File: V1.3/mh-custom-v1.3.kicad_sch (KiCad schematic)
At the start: 0 parts

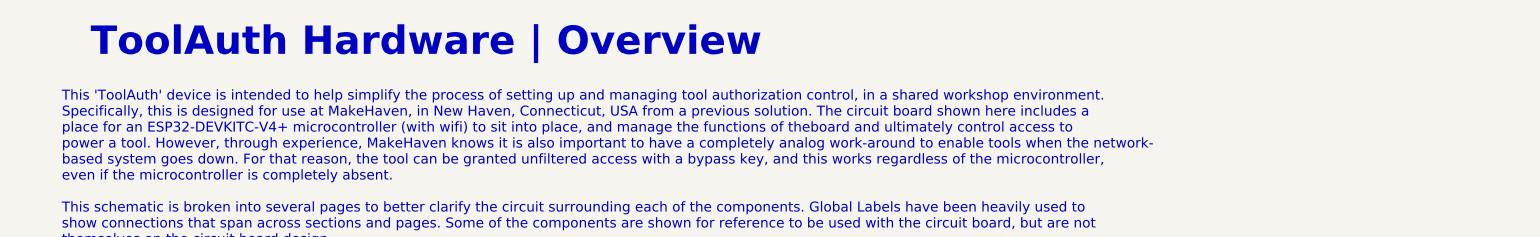
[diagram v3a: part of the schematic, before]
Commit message: clarify door-activator role || Active & Passive door operation
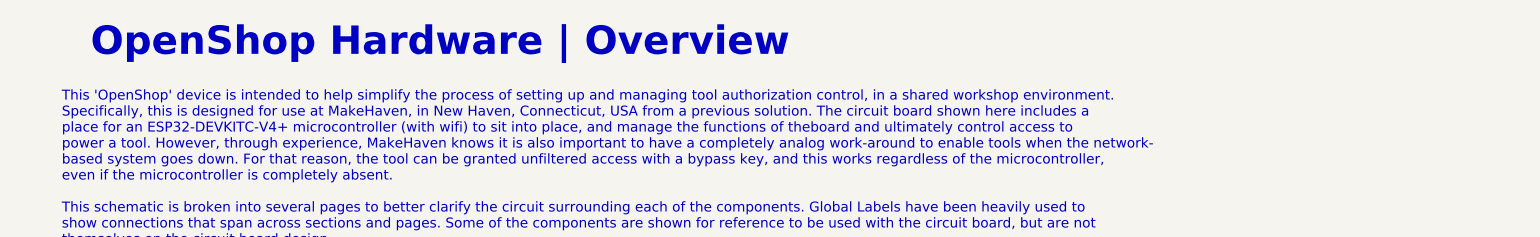
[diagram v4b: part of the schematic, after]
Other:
- note added: "OpenShop Hardware | Overview"
- note added: "This 'OpenShop' device is intended to help simplify the process of setting up and managing tool authorization control, in a shared workshop environment. Specifically, this is designed for use at MakeHaven, in New Haven, Connecticut, USA from a previous solution. The circuit board shown here includes a place for an ESP32-DEVKITC-V4+ microcontroller (with wifi) to sit into place, and manage the fun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"
- note removed: "This 'ToolAuth' device is intended to help simplify the process of setting up and managing tool authorization control, in a shared workshop environment. Specifically, this is designed for use at MakeHaven, in New Haven, Connecticut, USA from a previous solution. The circuit board shown here includes a place for an ESP32-DEVKITC-V4+ microcontroller (with wifi) to sit into place, and manage the fun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"
- note removed: "ToolAuth Hardware | Overview"
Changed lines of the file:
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@@
     (stroke (width 0) (type default) (color 0 0 0 0))
   )
-  (text "ToolAuth Hardware | Overview" (at 40.64 39.37 0)
+  (text "OpenShop Hardware | Overview" (at 40.64 39.37 0)
     (effects (font (size 5 5) (thickness 0.5) bold) (justify left bottom))
   )
@@
     (effects (font (size 1.75 1.75)) (justify left bottom))
   )
-  (text "This 'ToolAuth' device is intended to help simplify the process of setting up and managing tool authorization control, in a shared workshop environment. \nSpecifically, this is designed for use at MakeHaven, in New Haven, Connecticut, USA from a previous solution. The circuit board shown here includes a \nplace for an ESP32-DEVKITC-V4+ microcontroller (with wifi) to sit into place, and manage the functions of theboard and ultimately control access to \npower a tool. However, through experience, MakeHaven knows it is also important to have a completely analog work-around to enable tools when the network-\nbased system goes down. For that reason, the tool can be granted unfiltered access with a bypass key, and this works regardless of the microcontroller, \neven if the microcontroller is completely absent. \n\nThis schematic is broken into several pages to better clarify the circuit surrounding each of the components. Global Labels have been heavily used to \nshow connections that span across sections and pages. Some of the components are shown for reference to be used with the circuit board, but are not \nthemselves on the circuit board design. \n"
+  (text "This 'OpenShop' device is intended to help simplify the process of setting up and managing tool authorization control, in a shared workshop environment. \nSpecifically, this is designed for use at MakeHaven, in New Haven, Connecticut, USA from a previous solution. The circuit board shown here includes a \nplace for an ESP32-DEVKITC-V4+ microcontroller (with wifi) to sit into place, and manage the functions of theboard and ultimately control access to \npower a tool. However, through experience, MakeHaven knows it is also important to have a completely analog work-around to enable tools when the network-\nbased system goes down. For that reason, the tool can be granted unfiltered access with a bypass key, and this works regardless of the microcontroller, \neven if the microcontroller is completely absent. \n\nThis schematic is broken into several pages to better clarify the circuit surrounding each of the components. Global Labels have been heavily used to \nshow connections that span across sections and pages. Some of the components are shown for reference to be used with the circuit board, but are not \nthemselves on the circuit board design. \n"
     (at 35.56 72.39 0)
     (effects (font (size 1.75 1.75)) (justify left bottom))
